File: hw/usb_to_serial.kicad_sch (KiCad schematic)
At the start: 10 parts, among them P1 USB_C_Plug, U3 CH552E, U5 USBLC6-2SC6

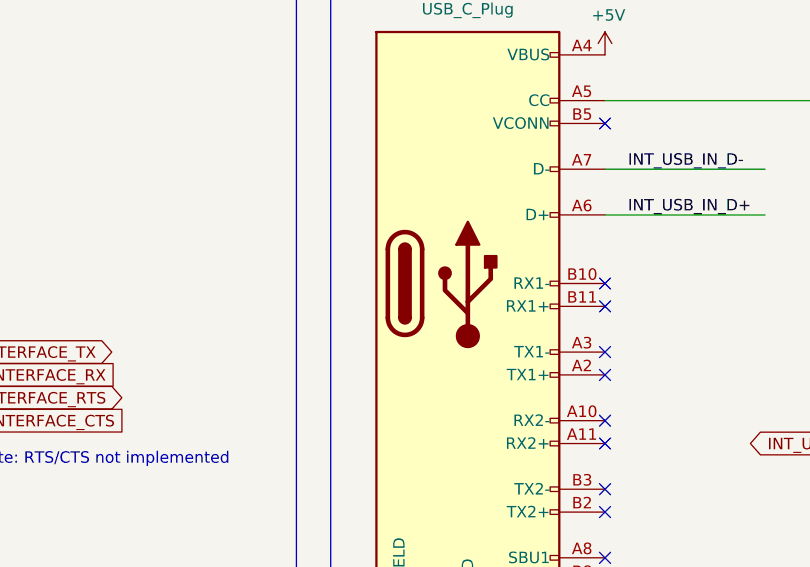
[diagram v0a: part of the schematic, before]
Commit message: Update project links to library
- Symbols
- Footprints
- Draw sheet
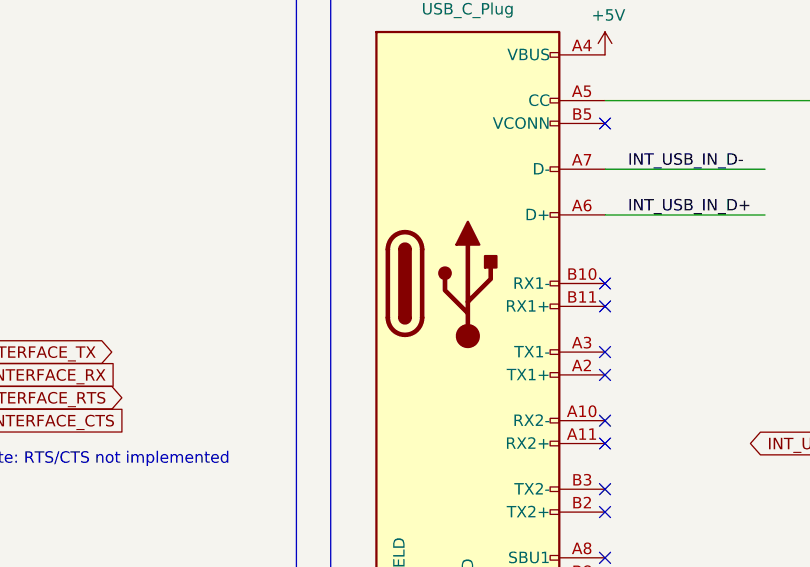
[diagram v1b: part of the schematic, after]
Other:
- title: USB-to-Serial Interface -> TK-1

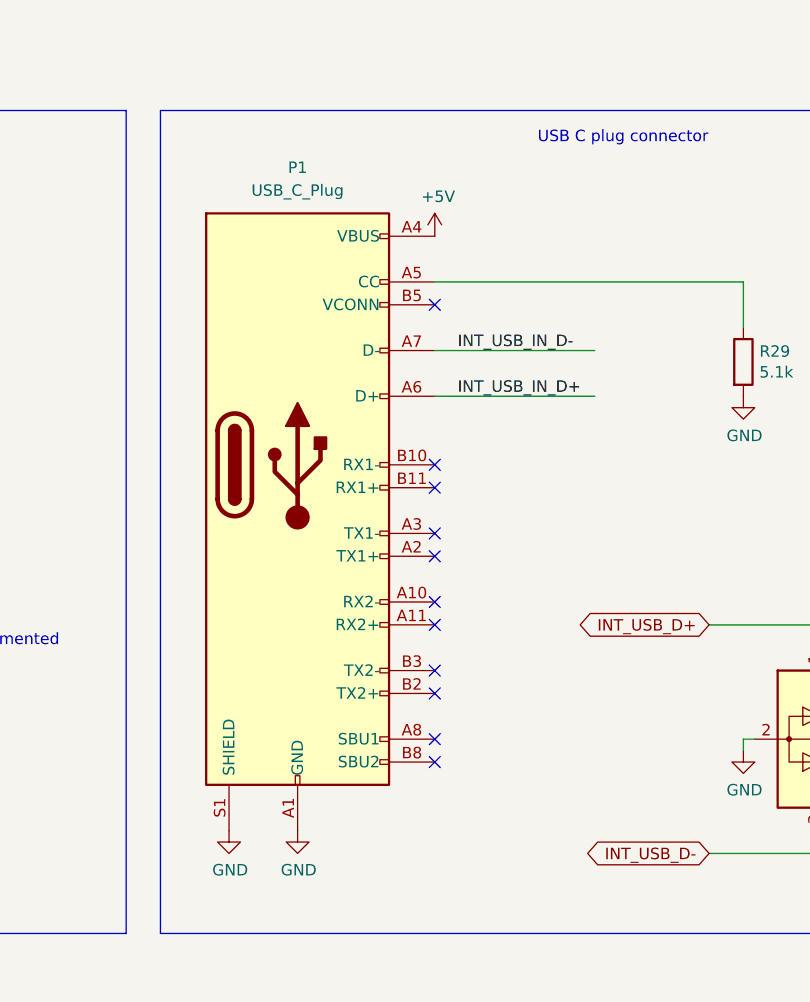
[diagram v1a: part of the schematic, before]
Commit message: Fix all ERC errors
- Update symbols
- Add PWR_FLAG
- Disable error on SPICE models
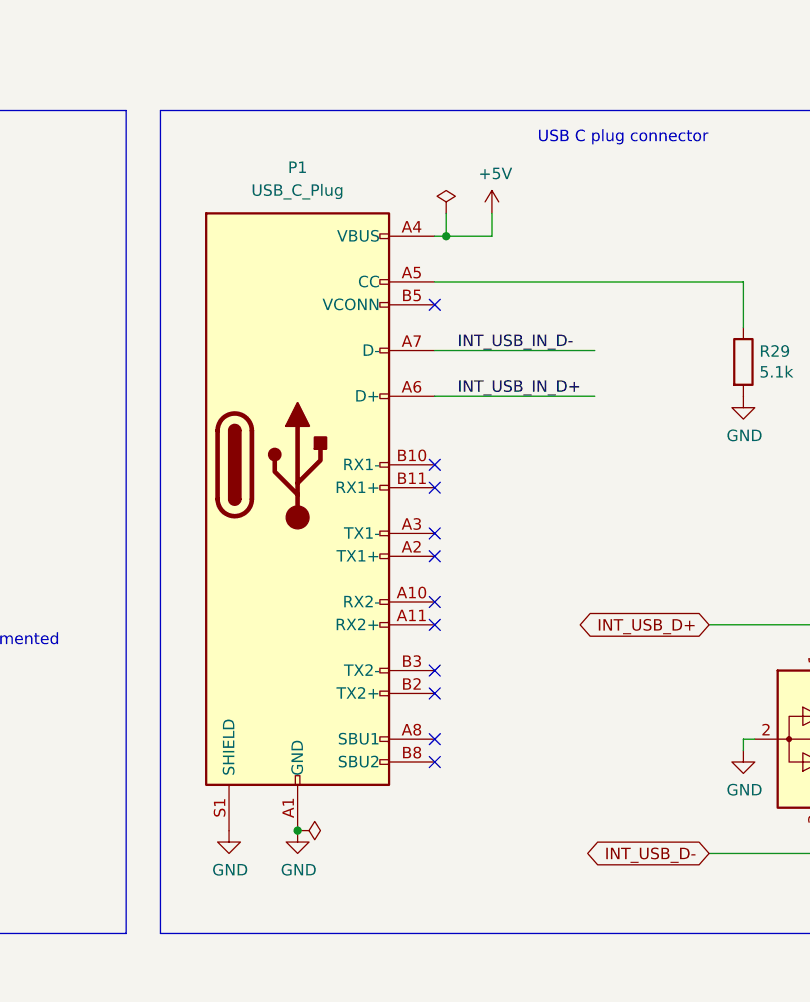
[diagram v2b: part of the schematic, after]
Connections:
- net +3V3 renamed +3.3V
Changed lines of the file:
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@@
   (junction (at 76.2 81.28) (diameter 0) (color 0 0 0 0)
+  )
+  (junction (at 207.01 57.15) (diameter 0) (color 0 0 0 0)
+  )
+  (junction (at 190.5 123.19) (diameter 0) (color 0 0 0 0)
   )
   (no_connect (at 205.74 92.71))
@@
     (stroke (width 0) (type default))
   )
+  (wire (pts (xy 207.01 54.61) (xy 207.01 57.15))
+    (stroke (width 0) (type default))
+  )
   (wire (pts (xy 92.71 100.33) (xy 101.6 100.33))
     (stroke (width 0) (type default))
@@
     (stroke (width 0) (type default))
   )
+  (wire (pts (xy 212.09 54.61) (xy 212.09 57.15))
+    (stroke (width 0) (type default))
+  )
   (wire (pts (xy 241.3 113.03) (xy 240.03 113.03))
     (stroke (width 0) (type default))
@@
     (stroke (width 0) (type default))
   )
+  (wire (pts (xy 207.01 57.15) (xy 205.74 57.15))
+    (stroke (width 0) (type default))
+  )
   (polyline (pts (xy 67.31 134.62) (xy 67.31 43.18))
+    (stroke (width 0) (type default))
+  )
+  (wire (pts (xy 212.09 57.15) (xy 207.01 57.15))
     (stroke (width 0) (type default))
   )
@@
     )
   )
+  (symbol (lib_id "power:PWR_FLAG") (at 207.01 54.61 0) (unit 1)
+    (in_bom yes) (on_board yes) (dnp no) (fields_autoplaced)
+    (property "Reference" "#FLG01" (at 207.01 52.705 0)
+      (effects (font (size 1.27 1.27)) hide)
+    )
+    (property "Value" "PWR_FLAG" (at 207.01 49.53 0)
+      (effects (font (size 1.27 1.27)) hide)
+    )
+    (property "Footprint" "" (at 207.01 54.61 0)
+      (effects (font (size 1.27 1.27)) hide)
+    )
+    (property "Datasheet" "~" (at 207.01 54.61 0)
+      (effects (font (size 1.27 1.27)) hide)
+    )
+    (pin "1")
+    (instances
+      (project "tk1"
+        (path "/8fc062a7-114d-48eb-a8f8-71128838f380/00000000-0000-0000-0000-00006161400b"
+          (reference "#FLG01") (unit 1)
+        )
+      )
+    )
+  )
   (symbol (lib_id "power:GND") (at 240.03 74.93 0) (unit 1)
     (in_bom yes) (on_board yes) (dnp no)
@@
         (path "/8fc062a7-114d-48eb-a8f8-71128838f380/00000000-0000-0000-0000-00006161400b"
           (reference "C7") (unit 1)
+        )
+      )
+    )
+  )
+  (symbol (lib_id "power:PWR_FLAG") (at 190.5 123.19 270) (unit 1)
+    (in_bom yes) (on_board yes) (dnp no) (fields_autoplaced)
+    (property "Reference" "#FLG02" (at 192.405 123.19 0)
+      (effects (font (size 1.27 1.27)) hide)
+    )
+    (property "Value" "PWR_FLAG" (at 195.58 123.19 0)
+      (effects (font (size 1.27 1.27)) hide)
+    )
+    (property "Footprint" "" (at 190.5 123.19 0)
+      (effects (font (size 1.27 1.27)) hide)
+    )
+    (property "Datasheet" "~" (at 190.5 123.19 0)
+      (effects (font (size 1.27 1.27)) hide)
+    )
+    (pin "1")
+    (instances
+      (project "tk1"
+        (path "/8fc062a7-114d-48eb-a8f8-71128838f380/00000000-0000-0000-0000-00006161400b"
+          (reference "#FLG02") (unit 1)
         )
       )
@@
     )
   )
-  (symbol (lib_id "power:+5V") (at 205.74 57.15 0) (unit 1)
-    (in_bom yes) (on_board yes) (dnp no)
-    (property "Reference" "#PWR0103" (at 205.74 60.96 0)
-      (effects (font (size 1.27 1.27)) hide)
-    )
-    (property "Value" "+5V" (at 206.121 52.7558 0)
-      (effects (font (size 1.27 1.27)))
-    )
-    (property "Footprint" "" (at 205.74 57.15 0)
-      (effects (font (size 1.27 1.27)) hide)
-    )
-    (property "Datasheet" "" (at 205.74 57.15 0)
-      (effects (font (size 1.27 1.27)) hide)
-    )
+  (symbol (lib_id "power:+5V") (at 212.09 54.61 0) (unit 1)
+    (in_bom yes) (on_board yes) (dnp no)
+    (property "Reference" "#PWR0103" (at 212.09 58.42 0)
+      (effects (font (size 1.27 1.27)) hide)
+    )
+    (property "Value" "+5V" (at 212.471 50.2158 0)
+      (effects (font (size 1.27 1.27)))
+    )
+    (property "Footprint" "" (at 212.09 54.61 0)
+      (effects (font (size 1.27 1.27)) hide)
+    )
+    (property "Datasheet" "" (at 212.09 54.61 0)
+      (effects (font (size 1.27 1.27)) hide)
+    )
